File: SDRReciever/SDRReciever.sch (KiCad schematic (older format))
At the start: 80 parts, among them J1 Conn_Coaxial, J10 I_0, J11 I_180, J12 Q_90, J13 Q_270, J14 I_OUT, J15 Q_OUT, J16 5V, J17 4.3V, J18 Conn_01x02_Female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

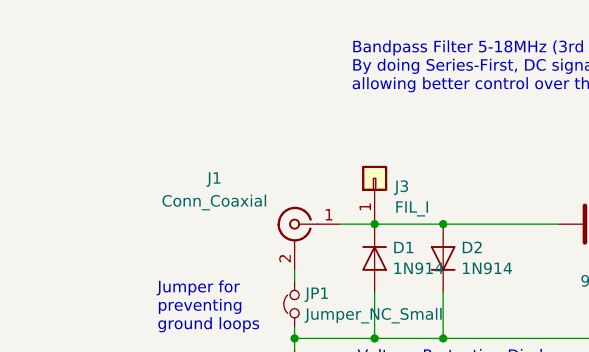
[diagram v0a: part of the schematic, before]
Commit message: Added images
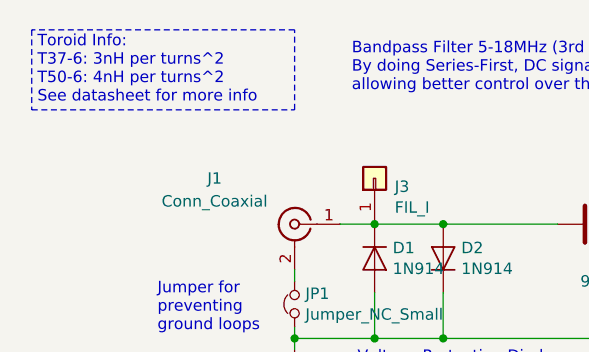
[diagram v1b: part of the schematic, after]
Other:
- note added: "Toroid Info:\nT37-6: 3nH per turns^2\nT50-6: 4nH per turns^2\nSee datasheet for more info"
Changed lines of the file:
@@
 Wire Wire Line
 	5600 6325 6300 6325
-$Comp
-L INA821ID:INA821ID U5
-U 1 1 5EA101A3
-P 5325 4650
-F 0 "U5" H 5175 4700 50  0000 L CNN
-F 1 "INA821ID" H 5075 4600 50  0000 L CNN
-F 2 "import_footprint:SOIC127P600X175-8N" H 5325 4650 50  0001 L BNN
-F 3 "B" H 5325 4650 50  0001 L BNN
-F 4 "1.75mm" H 5325 4650 50  0001 L BNN "Field4"
-F 5 "Texas Instruments" H 5325 4650 50  0001 L BNN "Field5"
-F 6 "IPC-7351B" H 5325 4650 50  0001 L BNN "Field6"
-	1    5325 4650
-	1    0    0    -1
-$EndComp
 Wire Wire Line
 	4925 4750 4925 4800
@@
 F 1 "INA821ID" H 5075 3300 50  0000 L CNN
 F 2 "import_footprint:SOIC127P600X175-8N" H 5325 3350 50  0001 L BNN
-F 3 "B" H 5325 3350 50  0001 L BNN
+F 3 "http://www.ti.com/lit/ds/symlink/ina821.pdf?HQS=TI-null-null-mousermode-df-pf-null-wwe&DCM=yes&ref_url=https%3A%2F%2Fwww.mouser.com%2F&distId=26" H 5325 3350 50  0001 L BNN
 F 4 "1.75mm" H 5325 3350 50  0001 L BNN "Field4"
 F 5 "Texas Instruments" H 5325 3350 50  0001 L BNN "Field5"
@@
 Wire Notes Line
 	4150 1850 4150 1700
+Text Notes 625  925  0    50   ~ 0
+Toroid Info:\nT37-6: 3nH per turns^2\nT50-6: 4nH per turns^2\nSee datasheet for more info
+Wire Notes Line
+	600  600  600  950
+Wire Notes Line
+	600  950  1750 950
+Wire Notes Line
+	1750 950  1750 600
+Wire Notes Line
+	1750 600  600  600
+$Comp
+L INA821ID:INA821ID U5
+U 1 1 5EA101A3
+P 5325 4650
+F 0 "U5" H 5175 4700 50  0000 L CNN
+F 1 "INA821ID" H 5075 4600 50  0000 L CNN
+F 2 "import_footprint:SOIC127P600X175-8N" H 5325 4650 50  0001 L BNN
+F 3 "B" H 5325 4650 50  0001 L BNN
+F 4 "1.75mm" H 5325 4650 50  0001 L BNN "Field4"
+F 5 "Texas Instruments" H 5325 4650 50  0001 L BNN "Field5"
+F 6 "IPC-7351B" H 5325 4650 50  0001 L BNN "Field6"
+	1    5325 4650
+	1    0    0    -1
+$EndComp
 $EndSCHEMATC
